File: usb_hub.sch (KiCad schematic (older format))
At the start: 25 parts, among them U1001 USB2422, Y1001 24MHz

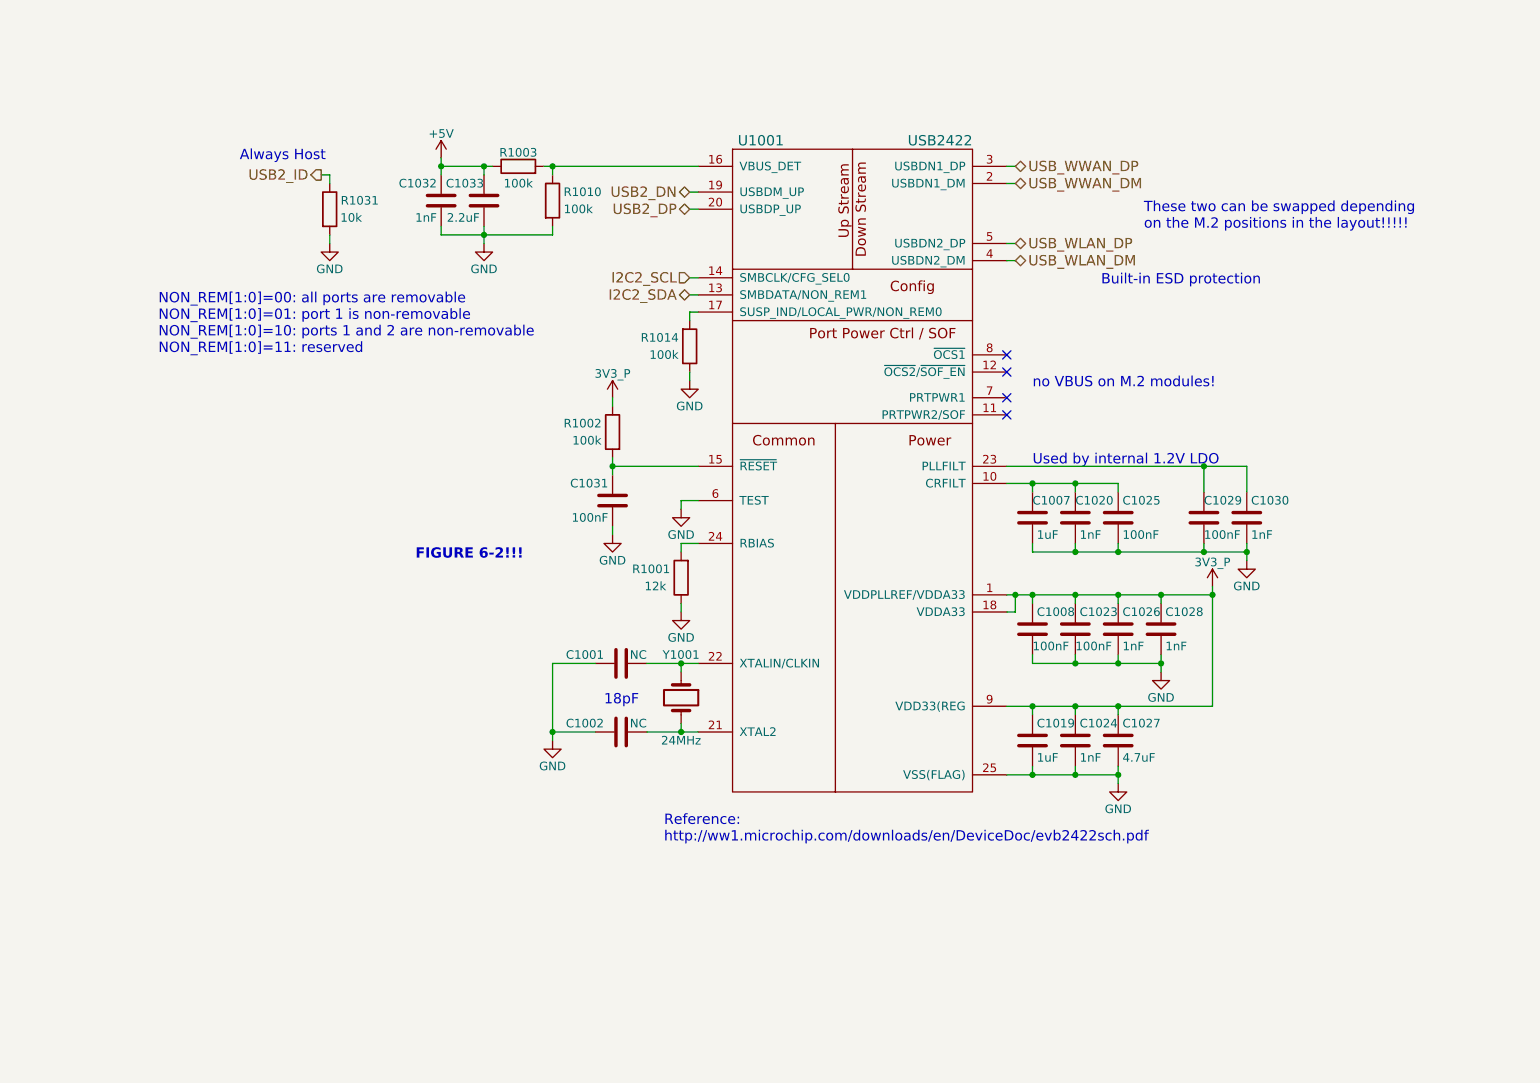
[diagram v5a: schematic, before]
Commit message: Begin WiFi+BT M.2 socket circuit, connect the associated USB bus from the hub circuit, determined that the i.MX8M's UART's default POR state is such that CTS is an output and RTS is an input and assigned the signals accordingly
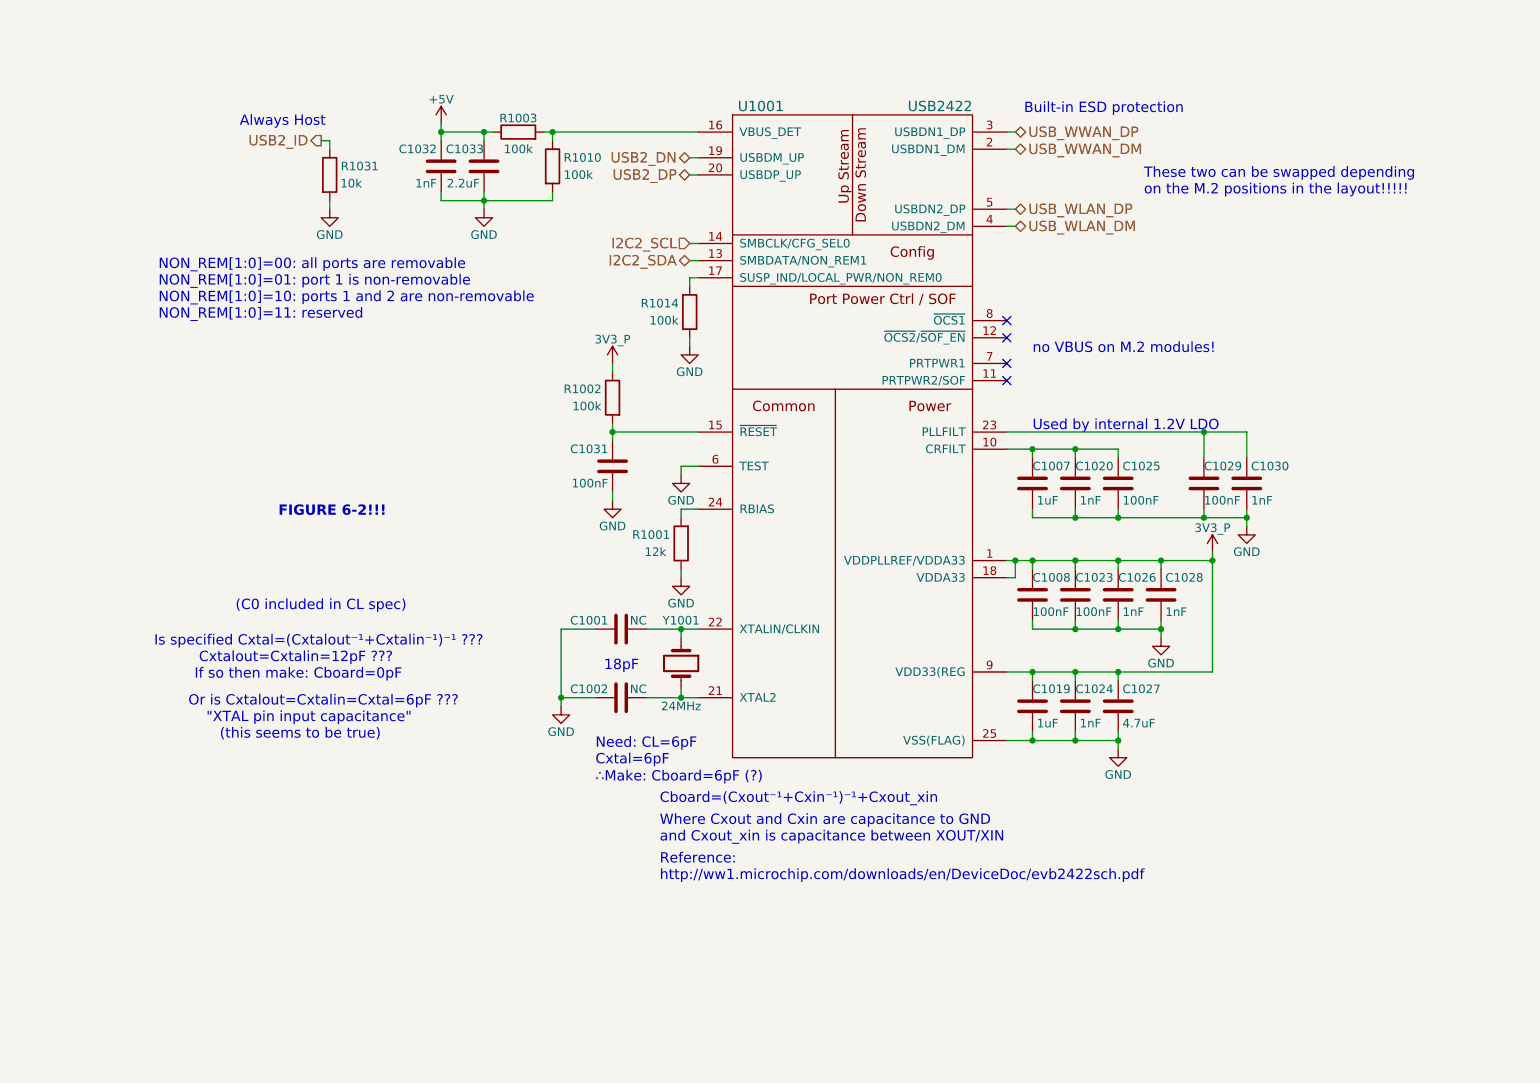
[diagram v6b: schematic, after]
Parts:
- Y1001: Distrib Link (none) -> https://www.digikey.com/product-detail/en/murata-electronic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; Distrib PN (none) -> 490-5576-1-ND; MFG Name (none) -> Murata; MFG Part Num (none) -> XRCGB24M000F3M00R0; Others (none) -> https://www.digikey.com/products/en/crystals-oscillators-re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; Tolerance (none) -> -
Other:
- note added: "(C0 included in CL spec)"
- note added: "Cboard=(Cxout⁻¹+Cxin⁻¹)⁻¹+Cxout_xin"
- note added: "Is specified Cxtal=(Cxtalout⁻¹+Cxtalin⁻¹)⁻¹ ???\n Cxtalout=Cxtalin=12pF ???\n If so then make: Cboard=0pF"
- note added: "Need: CL=6pF\nCxtal=6pF"
- note added: "Or is Cxtalout=Cxtalin=Cxtal=6pF ???\n "XTAL pin input capacitance"\n (this seems to be true)"
- note added: "Where Cxout and Cxin are capacitance to GND\nand Cxout_xin is capacitance between XOUT/XIN"
- note added: "∴Make: Cboard=6pF (?)"
- moved on the sheet: C1001, C1002, C1007, C1008, C1019, C1020, C1023, C1024, C1025, C1026, C1027, C1028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
